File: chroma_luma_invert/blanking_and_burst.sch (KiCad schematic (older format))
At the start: 33 parts

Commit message: routing boards
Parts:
- C2, C3, C4, C5, C6, C7: renamed from C?; footprint (none) -> Capacitor_THT:C_Disc_D4.7mm_W2.5mm_P5.00mm
- R16, R17, R18, R19, R20, R21, R22, R23, R24, R25, R26, R27: renamed from R?; footprint (none) -> Resistor_THT:R_Axial_DIN0207_L6.3mm_D2.5mm_P7.62mm_Horizontal
- RV1, RV2, RV3, RV4: renamed from RV?; footprint (none) -> lib_fp:Pot_trim_3362_tayda
- U10, U7, U8: renamed from U?; footprint (none) -> Package_DIP:DIP-16_W7.62mm_LongPads; symbol custom:74HC4538 -> symbol:74HC4538
- U5, U6: renamed from U?; footprint (none) -> Package_DIP:DIP-8_W7.62mm_LongPads
- U9: renamed from U?; footprint (none) -> Package_DIP:DIP-16_W7.62mm_LongPads

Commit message: updated two_comparator and added two_point_one
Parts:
- removed U5, U6: LM311, Package_DIP:DIP-8_W7.62mm_LongPads, symbol Comparator:LM311
- added U2: LM393, Package_DIP:DIP-8_W7.62mm_LongPads, symbol Comparator:LM393
- R21: value 10k -> 3.9k
- R22: value 3.9k -> 10k
- renumbered U10 to U5, U9 to U6
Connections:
- net +5V: now also U8.5 (~A), U2.8 (V+)
- net 2.5V: now also U2.5 (+)
- net GND: now also U2.4 (V-); no longer U8.4 (B)
- net original_video: now also U2.3 (+)
- net sync: now also U6.10 (CLK), U2.1; no longer U6.11 (Reset)
- net v_sync: now also U6.11 (Reset), U2.7; no longer U6.10 (CLK)
- net at R21.2, R22.2: now also U2.2 (-)
- net at C3.1, U7.1 (Cx): no longer R18.1
- net at C3.2, U7.2 (RxCx): now also R18.1
- net at C4.2, R20.2: now also U2.6 (_)
- net at C2.1, U7.15 (Cx): no longer R16.1
- net at C2.2, U7.14 (RxCx): now also R16.1
- net at U6.12 (Q8): now also U8.4 (B); no longer U8.5 (~A)
- net at C7.1, U8.1 (Cx): no longer R26.1
- net at C7.2, U8.2 (RxCx): now also R26.1
- net at C6.1, U8.15 (Cx): no longer R25.1
- net at C6.2, U8.14 (RxCx): now also R25.1
- net at C5.1, U5.1 (Cx): no longer R24.1
- net at C5.2, U5.2 (RxCx): now also R24.1
- no-connect marks 24 -> 20
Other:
- note added: "RV4, RV3 and R25 value depends on ntsc/pal"
- moved on the sheet: R16, R18, R19, R24, R25, R26, RV1, RV2, RV3, RV4, U6

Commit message: revised all boards
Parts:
- RV1: value 10k_pot -> 10k_trim; footprint lib_fp:Pot_trim_3362_tayda -> lib_fp:tht_vertical_trimpot_3362
- RV2: value 5k_pot -> 5k_trim; footprint lib_fp:Pot_trim_3362_tayda -> lib_fp:tht_vertical_trimpot_3362
- RV3: value 100k_pot -> 100k_trim; footprint lib_fp:Pot_trim_3362_tayda -> lib_fp:tht_vertical_trimpot_3362
- RV4: value 20k_pot -> 20k_trim; footprint lib_fp:Pot_trim_3362_tayda -> lib_fp:tht_vertical_trimpot_3362
- U6: value 4040 -> CD4040
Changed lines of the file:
@@
 P 7625 1100
 F 0 "RV2" V 7418 1100 50  0000 C CNN
-F 1 "5k_pot" V 7509 1100 50  0000 C CNN
-F 2 "lib_fp:Pot_trim_3362_tayda" H 7625 1100 50  0001 C CNN
+F 1 "5k_trim" V 7509 1100 50  0000 C CNN
+F 2 "lib_fp:tht_vertical_trimpot_3362" H 7625 1100 50  0001 C CNN
 F 3 "~" H 7625 1100 50  0001 C CNN
 	1    7625 1100
@@
 P 9100 875
 F 0 "RV1" V 8893 875 50  0000 C CNN
-F 1 "10k_pot" V 8984 875 50  0000 C CNN
-F 2 "lib_fp:Pot_trim_3362_tayda" H 9100 875 50  0001 C CNN
+F 1 "10k_trim" V 8984 875 50  0000 C CNN
+F 2 "lib_fp:tht_vertical_trimpot_3362" H 9100 875 50  0001 C CNN
 F 3 "~" H 9100 875 50  0001 C CNN
 	1    9100 875
@@
 P 6000 5175
 F 0 "U6" H 6100 6025 50  0000 C CNN
-F 1 "4040" H 6150 5925 50  0000 C CNN
+F 1 "CD4040" H 6150 5925 50  0000 C CNN
 F 2 "Package_DIP:DIP-16_W7.62mm_LongPads" H 6000 5175 50  0001 C CNN
 F 3 "http://www.intersil.com/content/dam/Intersil/documents/cd40/cd4020bms-24bms-40bms.pdf" H 6000 5175 50  0001 C CNN
@@
 P 7100 4525
 F 0 "RV4" V 6893 4525 50  0000 C CNN
-F 1 "20k_pot" V 6984 4525 50  0000 C CNN
-F 2 "lib_fp:Pot_trim_3362_tayda" H 7100 4525 50  0001 C CNN
+F 1 "20k_trim" V 6984 4525 50  0000 C CNN
+F 2 "lib_fp:tht_vertical_trimpot_3362" H 7100 4525 50  0001 C CNN
 F 3 "~" H 7100 4525 50  0001 C CNN
 	1    7100 4525
@@
 P 8575 4350
 F 0 "RV3" V 8368 4350 50  0000 C CNN
-F 1 "100k_pot" V 8459 4350 50  0000 C CNN
-F 2 "lib_fp:Pot_trim_3362_tayda" H 8575 4350 50  0001 C CNN
+F 1 "100k_trim" V 8459 4350 50  0000 C CNN
+F 2 "lib_fp:tht_vertical_trimpot_3362" H 8575 4350 50  0001 C CNN
 F 3 "~" H 8575 4350 50  0001 C CNN
 	1    8575 4350

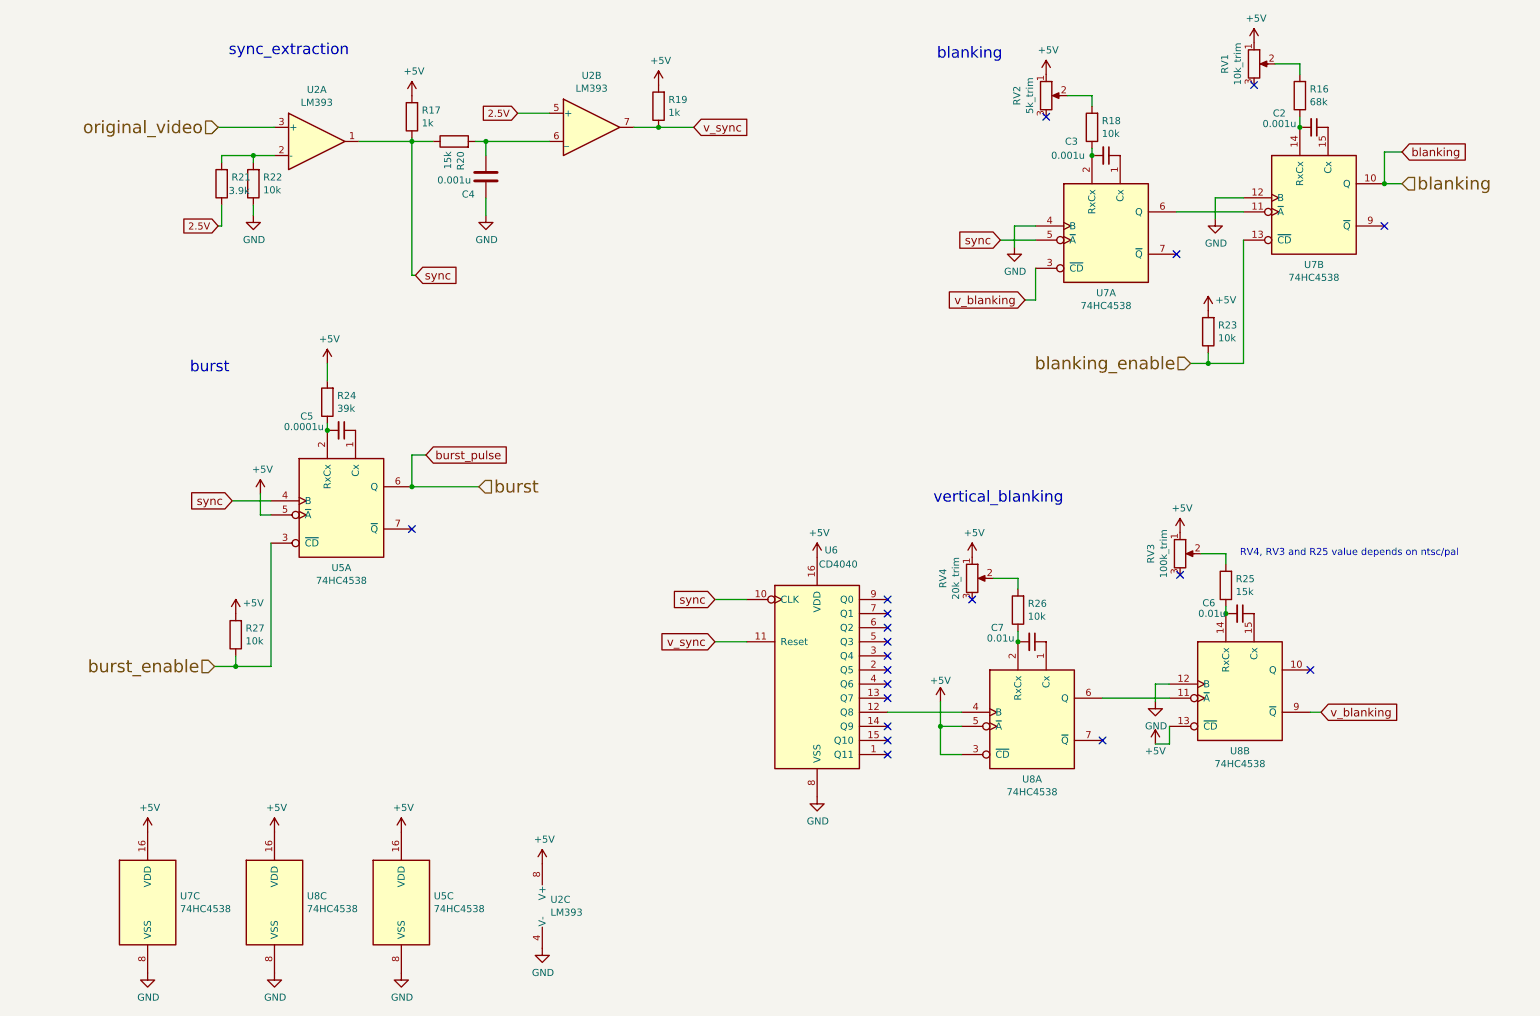
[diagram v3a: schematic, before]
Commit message: update for new chroma_luma circuit
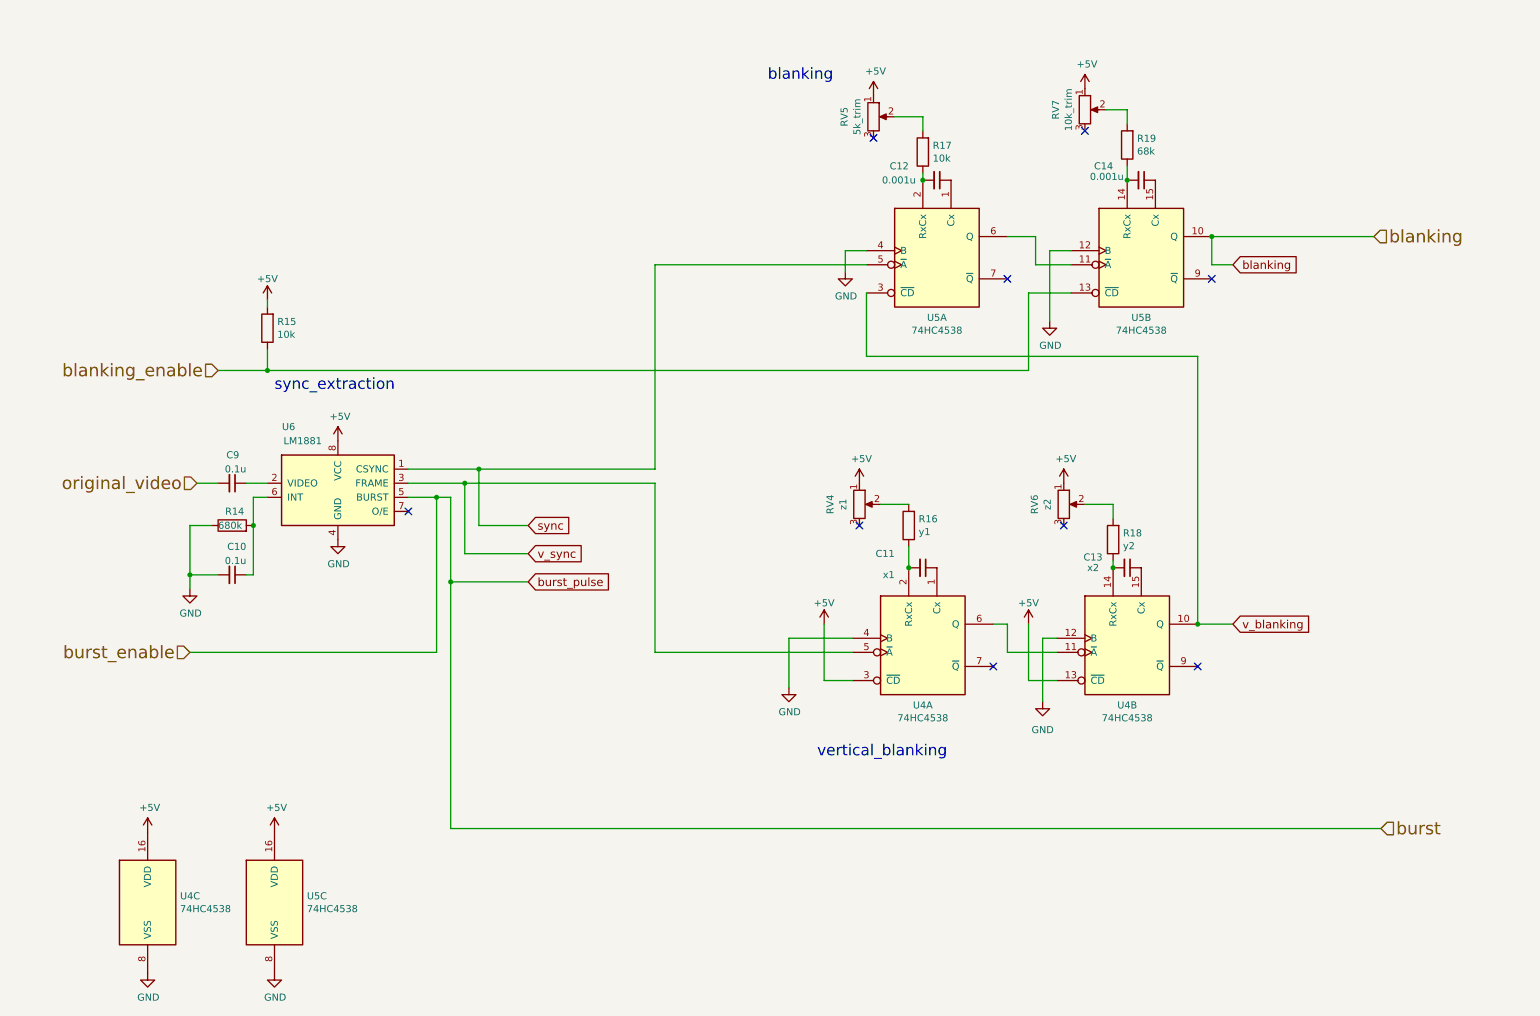
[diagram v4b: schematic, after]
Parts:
- removed C4: 0.001u, Capacitor_THT:C_Disc_D4.7mm_W2.5mm_P5.00mm, symbol Device:C
- removed C5: 0.0001u, Capacitor_THT:C_Disc_D4.7mm_W2.5mm_P5.00mm, symbol Device:C_Small
- removed R17, R19: 1k, Resistor_THT:R_Axial_DIN0207_L6.3mm_D2.5mm_P7.62mm_Horizontal, symbol Device:R
- removed R20: 15k, Resistor_THT:R_Axial_DIN0207_L6.3mm_D2.5mm_P7.62mm_Horizontal, symbol Device:R
- removed R21: 3.9k, Resistor_THT:R_Axial_DIN0207_L6.3mm_D2.5mm_P7.62mm_Horizontal, symbol Device:R
- removed R22, R27: 10k, Resistor_THT:R_Axial_DIN0207_L6.3mm_D2.5mm_P7.62mm_Horizontal, symbol Device:R
- removed R24: 39k, Resistor_THT:R_Axial_DIN0207_L6.3mm_D2.5mm_P7.62mm_Horizontal, symbol Device:R
- removed U2: LM393, Package_DIP:DIP-8_W7.62mm_LongPads, symbol Comparator:LM393
- removed U5: 74HC4538, Package_DIP:DIP-16_W7.62mm_LongPads, symbol symbol:74HC4538
- removed U6: CD4040, Package_DIP:DIP-16_W7.62mm_LongPads, symbol 4xxx:4040
- added C10, C9: 0.1u, Capacitor_THT:C_Disc_D4.7mm_W2.5mm_P5.00mm, symbol Device:C_Small
- added R14: 680k, Resistor_THT:R_Axial_DIN0207_L6.3mm_D2.5mm_P7.62mm_Horizontal, symbol Device:R
- added U6: LM1881, symbol Video:LM1881
- C11: renamed from C7; value 0.01u -> x1
- C13: renamed from C6; value 0.01u -> x2
- R16: renamed from R26; value 10k -> y1
- R18: renamed from R25; value 15k -> y2
- RV4: value 20k_trim -> z1
- RV6: renamed from RV3; value 100k_trim -> z2
- renumbered C3 to C12, C2 to C14, R23 to R15, R18 to R17, R16 to R19, RV2 to RV5, RV1 to RV7, U8 to U4, U7 to U4, U7 to U5, U8 to U5
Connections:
- net +5V: now also U6.8 (VCC); no longer U4.5 (~A)
- net GND: now also U4.4 (B), C10.2, R14.1, U6.4 (GND)
- net burst_pulse: now also U6.5 (BURST)
- net original_video: now also C9.2
- net sync: now also U6.1 (CSYNC)
- net v_blanking: now also U4.10 (Q); no longer U4.9 (~Q)
- net v_sync: now also U4.5 (~A), U6.3 (FRAME)
- new net: C9.1, U6.2 (VIDEO)
- new net: C10.1, R14.2, U6.6 (INT)
- no-connect marks 20 -> 9
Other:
- note removed: "RV4, RV3 and R25 value depends on ntsc/pal"
- note removed: "burst"
- moved on the sheet: C11, C12, C13, C14, R15, R16, R17, R18, R19, RV4, RV5, RV6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

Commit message: working on nexr version for colorizer and inverter
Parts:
- C11: value x1 -> 0.1uf
- C13: value x2 -> 1uf
- R16: value y1 -> 12k
- R18: value y2 -> 22k
- RV4: value z1 -> 10k_trim
- RV6: value z2 -> 10k_trim
- U6: footprint (none) -> lib_fp:DIP-SOIC-8
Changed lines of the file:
@@
 $Descr A4 11693 8268
 encoding utf-8
-Sheet 2 2
+Sheet 2 3
 Title ""
 Date ""
@@
 P 6300 4000
 F 0 "RV4" V 6093 4000 50  0000 C CNN
-F 1 "z1" V 6184 4000 50  0000 C CNN
+F 1 "10k_trim" V 6184 4000 50  0000 C CNN
 F 2 "lib_fp:tht_vertical_trimpot_3362" H 6300 4000 50  0001 C CNN
 F 3 "~" H 6300 4000 50  0001 C CNN
@@
 P 8100 4250
 F 0 "R18" H 8030 4204 50  0000 R CNN
-F 1 "y2" H 8030 4295 50  0000 R CNN
+F 1 "22k" H 8030 4295 50  0000 R CNN
 F 2 "Resistor_THT:R_Axial_DIN0207_L6.3mm_D2.5mm_P7.62mm_Horizontal" V 8030 4250 50  0001 C CNN
 F 3 "~" H 8100 4250 50  0001 C CNN
@@
 P 7750 4000
 F 0 "RV6" V 7543 4000 50  0000 C CNN
-F 1 "z2" V 7634 4000 50  0000 C CNN
+F 1 "10k_trim" V 7634 4000 50  0000 C CNN
 F 2 "lib_fp:tht_vertical_trimpot_3362" H 7750 4000 50  0001 C CNN
 F 3 "~" H 7750 4000 50  0001 C CNN
@@
 P 8200 4450
 F 0 "C13" V 8125 4275 50  0000 R CNN
-F 1 "x2" V 8200 4250 50  0000 R CNN
+F 1 "1uf" V 8200 4250 50  0000 R CNN
 F 2 "Capacitor_THT:C_Disc_D4.7mm_W2.5mm_P5.00mm" H 8238 4300 50  0001 C CNN
 F 3 "~" H 8200 4450 50  0001 C CNN
@@
 P 6750 4450
 F 0 "C11" V 6650 4250 50  0000 R CNN
-F 1 "x1" V 6800 4250 50  0000 R CNN
+F 1 "0.1uf" V 6800 4250 50  0000 R CNN
 F 2 "Capacitor_THT:C_Disc_D4.7mm_W2.5mm_P5.00mm" H 6788 4300 50  0001 C CNN
 F 3 "~" H 6750 4450 50  0001 C CNN
@@
 P 6650 4150
 F 0 "R16" H 6580 4104 50  0000 R CNN
-F 1 "y1" H 6580 4195 50  0000 R CNN
+F 1 "12k" H 6580 4195 50  0000 R CNN
 F 2 "Resistor_THT:R_Axial_DIN0207_L6.3mm_D2.5mm_P7.62mm_Horizontal" V 6580 4150 50  0001 C CNN
 F 3 "~" H 6650 4150 50  0001 C CNN
@@
 F 0 "U6" H 2250 4450 50  0000 C CNN
 F 1 "LM1881" H 2350 4350 50  0000 C CNN
-F 2 "" H 2600 3950 50  0001 C CNN
+F 2 "lib_fp:DIP-SOIC-8" H 2600 3950 50  0001 C CNN
 F 3 "" H 2600 3950 50  0001 C CNN
 	1    2600 3950
